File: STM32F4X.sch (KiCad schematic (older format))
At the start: 19 parts

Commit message: Added USB
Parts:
- added D?: LED, symbol Device:LED
- added J?: SWD_Conn, symbol Connector_Generic:Conn_02x05_Odd_Even
- added J?: USB_B_Micro, symbol Connector:USB_B_Micro
- added R?: 2K2, symbol Device:R_Small
- added U?: USBLC6-2SC6, Package_TO_SOT_SMD:SOT-23-6, symbol Power_Protection:USBLC6-2SC6
- R?: value 1K -> 2K2
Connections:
- net labels added: +5V, BOOT1, USB_CONN_DM, USB_CONN_DP
- wire segments 77 -> 94
- no-connect marks 0 -> 4
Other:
- note added: "SWD"
- note added: "USB Connection"
- moved on the sheet: C?, D?, R?, SW?, U?

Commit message: Initial board layout
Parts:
- removed C?: 2.2uF, symbol Device:C_Small
- removed D?: RED, symbol Device:LED_Small
- removed R?: 2K2, symbol Device:R_Small
- added C1, C10, C17: 100nF, Capacitor_SMD:C_0805_2012Metric_Pad1.18x1.45mm_HandSolder, symbol Device:C_Small
- added C2: 4.7uF, Capacitor_SMD:C_0805_2012Metric_Pad1.18x1.45mm_HandSolder, symbol Device:C_Small
- added C3: 10uF, Capacitor_SMD:C_0805_2012Metric_Pad1.18x1.45mm_HandSolder, symbol Device:C_Small
- added C4: 2.2uF, Capacitor_SMD:C_0805_2012Metric_Pad1.18x1.45mm_HandSolder, symbol Device:C_Small
- added D1, D3: B260A-13-F, Diode_SMD:D_0805_2012Metric_Pad1.15x1.40mm_HandSolder, symbol Device:D_Schottky
- added D2: LED_Small, LED_SMD:LED_0805_2012Metric_Pad1.15x1.40mm_HandSolder, symbol Device:LED_Small
- added F1, F2, F3: 500mA, Fuse:Fuse_1206_3216Metric_Pad1.42x1.75mm_HandSolder, symbol Device:Polyfuse_Small
- added J1: POW_IN, TerminalBlock:TerminalBlock_Wuerth_691311400102_P7.62mm, symbol Connector:Screw_Terminal_01x02
- added J4: Micro_SD_Card, Connector_Card:microSD_HC_Molex_104031-0811, symbol Connector:Micro_SD_Card
- added L1: 22uH, Inductor_SMD:L_1206_3216Metric_Pad1.42x1.75mm_HandSolder, symbol Device:L_Small
- added R1: 49.9K, Resistor_SMD:R_0805_2012Metric_Pad1.20x1.40mm_HandSolder, symbol Device:R_Small
- added R2: 15.8K, Resistor_SMD:R_0805_2012Metric_Pad1.20x1.40mm_HandSolder, symbol Device:R_Small
- added R3: 68K, Resistor_SMD:R_0805_2012Metric_Pad1.20x1.40mm_HandSolder, symbol Device:R_Small
- added R4: 2K2, Resistor_SMD:R_0805_2012Metric_Pad1.20x1.40mm_HandSolder, symbol Device:R_Small
- added U1: AOZ1282CI, Package_TO_SOT_SMD:SOT-23-6, symbol Regulator_Switching:AOZ1282CI
- C11, C12, C13, C14, C15, C16, C5, C6, C7, C8, C9: renamed from C?; footprint (none) -> Capacitor_SMD:C_0805_2012Metric_Pad1.18x1.45mm_HandSolder
- D4: renamed from D?; footprint (none) -> LED_SMD:LED_0805_2012Metric_Pad1.15x1.40mm_HandSolder
- FB1: renamed from FB?; footprint (none) -> Inductor_SMD:L_0805_2012Metric_Pad1.15x1.40mm_HandSolder
- J2: renamed from J?; footprint (none) -> Connector_USB:USB_Micro-B_Molex-105017-0001; symbol Connector:USB_B_Micro -> STM32F4X-rescue:USB_B_Micro-Connector
- J3: renamed from J?; footprint (none) -> Connector_PinHeader_2.54mm:PinHeader_2x05_P2.54mm_Vertical
- R5, R6: renamed from R?; footprint (none) -> Resistor_SMD:R_0805_2012Metric_Pad1.20x1.40mm_HandSolder
- SW1: renamed from SW?; footprint (none) -> digikey-footprints:Switch_Slide_11.6x4mm_EG1218
- U3: renamed from U?; symbol Power_Protection:USBLC6-2SC6 -> STM32F4X-rescue:USBLC6-2SC6-Power_Protection
- Y1: renamed from Y?; footprint (none) -> Oscillator:Oscillator_SMD_EuroQuartz_XO32-4Pin_3.2x2.5mm_HandSoldering
- gave numbers to parts that had none: 1
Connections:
- net labels added: BST, BUCK_OUT, FB, SDIO_CK, SDIO_CMD, SDIO_D0, SDIO_D1, SDIO_D2, SDIO_D3, SPI_CS, SPI_MISO, SPI_MOSI, SPI_SCLK, VBUS, VCC
- net labels removed: BOOT1, I2C2_SCL, I2C2_SDA, UART5_RX, UART5_TX
- wire segments 94 -> 134
- no-connect marks 4 -> 9
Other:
- note added: "Power Supply"
- note added: "SD_Card"
- note added: "The output voltage of the buck converter is set by:\n V_out = 0.8*(1+R1/R2)"
- moved on the sheet: C11, C12, C13, C14, C15, C16, C5, C6, C7, C8, C9, D4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

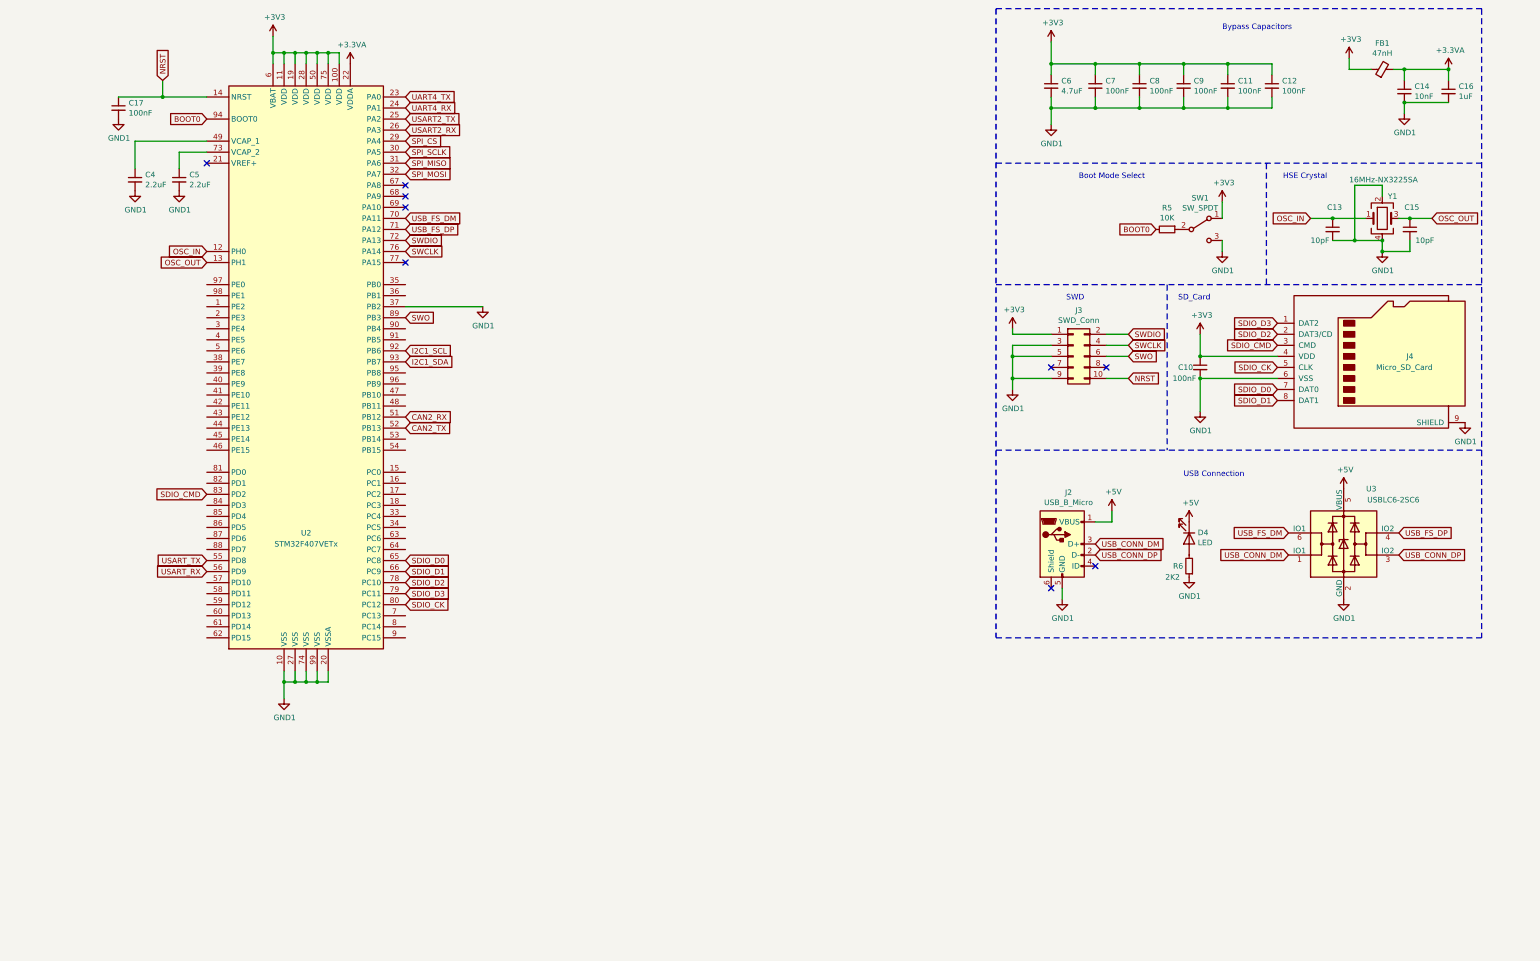
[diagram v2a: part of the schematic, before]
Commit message: Removed pcb layout. Adding more functionality
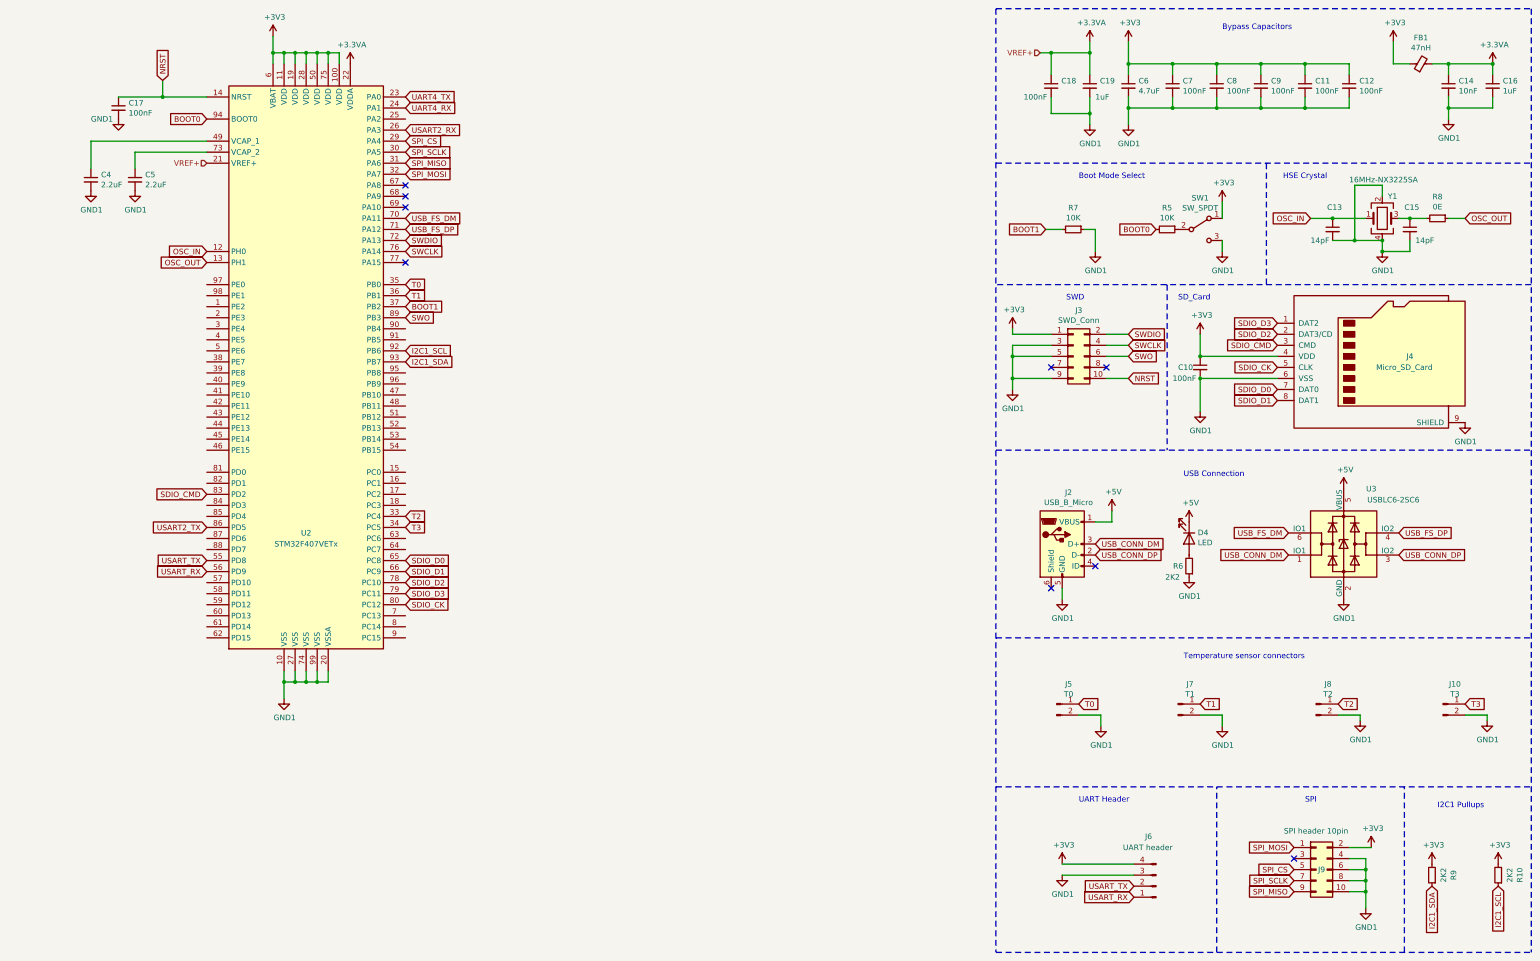
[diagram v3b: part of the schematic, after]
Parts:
- added C18: 100nF, Capacitor_SMD:C_0805_2012Metric_Pad1.18x1.45mm_HandSolder, symbol Device:C_Small
- added C19: 1uF, Capacitor_SMD:C_0805_2012Metric_Pad1.18x1.45mm_HandSolder, symbol Device:C_Small
- added J10: T3, symbol Connector:Conn_01x02_Male
- added J5: T0, symbol Connector:Conn_01x02_Male
- added J6: UART header, symbol Connector:Conn_01x04_Male
- added J7: T1, symbol Connector:Conn_01x02_Male
- added J8: T2, symbol Connector:Conn_01x02_Male
- added J9: SPI header 10pin, symbol Connector_Generic:Conn_02x05_Odd_Even
- added R10, R9: 2K2, Resistor_SMD:R_0805_2012Metric_Pad1.20x1.40mm_HandSolder, symbol Device:R_Small
- added R7: 10K, Resistor_SMD:R_0805_2012Metric_Pad1.20x1.40mm_HandSolder, symbol Device:R_Small
- added R8: 0E, Resistor_SMD:R_0805_2012Metric_Pad1.20x1.40mm_HandSolder, symbol Device:R_Small
- C13, C15: value 10pF -> 14pF
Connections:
- net +3.3VA: now also U2.21 (VREF+), C18.1, C19.1
- net +3V3: now also J6.4 (Pin_4), J9.2 (Pin_2), R10.2, R9.2
- net GND1: now also C18.2, C19.2, J10.2 (Pin_2), J5.2 (Pin_2), J6.3 (Pin_3), J7.2 (Pin_2), J8.2 (Pin_2), J9.10 (Pin_10), J9.4 (Pin_4), J9.6 (Pin_6), J9.8 (Pin_8), R7.1; no longer U2.37 (PB2)
- net I2C1_SCL: now also R10.1
- net I2C1_SDA: now also R9.1
- net OSC_OUT: now also R8.1; no longer C15.1, Y1.3
- net SPI_CS: now also J9.5 (Pin_5)
- net SPI_MISO: now also J9.9 (Pin_9)
- net SPI_MOSI: now also J9.1 (Pin_1)
- net SPI_SCLK: now also J9.7 (Pin_7)
- net USART2_TX: now also U2.86 (PD5); no longer U2.25 (PA2)
- net USART_RX: now also J6.1 (Pin_1)
- net USART_TX: now also J6.2 (Pin_2)
- net T2: now reaches U2.33 (PC4)
- net T2: now also J8.1 (Pin_1)
- net T3: now reaches U2.34 (PC5)
- net T3: now also J10.1 (Pin_1)
- net T0: now reaches U2.35 (PB0)
- net T0: now also J5.1 (Pin_1)
- net T1: now reaches U2.36 (PB1)
- net T1: now also J7.1 (Pin_1)
- net CAN2_RX: no longer names the net of U2.51 (PB12)
- net CAN2_TX: no longer names the net of U2.52 (PB13)
- new net: C15.1, R8.2, Y1.3
- new net BOOT1: R7.2, U2.37 (PB2)
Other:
- note added: "I2C1 Pullups\n"
- note added: "SPI\n"
- note added: "Temperature sensor connectors"
- note added: "UART Header\n"
- moved on the sheet: C11, C12, C14, C16, C4, C5, C6, C7, C8, C9, FB1

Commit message: Added, a proper 3v3 LDO from buck converter output. Started allocation for SPI and UART pins for motor drivers.
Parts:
- added A?: DRV8825_X, Module:Pololu_Breakout-16_15.2x20.3mm, symbol Driver_Motor:Pololu_Breakout_DRV8825
- added A?: A4988_Y, Module:Pololu_Breakout-16_15.2x20.3mm, symbol Driver_Motor:Pololu_Breakout_A4988
- added A?: Pololu_Breakout_TMC2209, Module:Pololu_Breakout-16_15.2x20.3mm, symbol Trinamic_breakout:Pololu_Breakout_TMC2209
- added A?: Pololu_Breakout_TMC2130, Module:Pololu_Breakout-16_15.2x20.3mm, symbol Trinamic_breakout:Pololu_Breakout_TMC2130
- added C20, C21, C22, C23, C24, C25: 10uF, Capacitor_SMD:C_0805_2012Metric_Pad1.18x1.45mm_HandSolder, symbol Device:C_Small
- added C? (x3): 100uF, 65V, symbol Device:CP_Small
- added C? (x2): 1uF, Capacitor_SMD:C_0805_2012Metric_Pad1.18x1.45mm_HandSolder, symbol Device:C_Small
- added J11: TC, symbol Connector:Conn_01x02_Male
- added J12: T3, symbol Connector:Conn_01x02_Male
- added J? (x3): Motor, symbol Connector:Conn_01x04_Female
- added R11, R12, R13, R14, R15, R16, R17, R? (x3): 10K, Resistor_SMD:R_0805_2012Metric_Pad1.20x1.40mm_HandSolder, symbol Device:R_Small
- added R18: 1M, Resistor_SMD:R_0805_2012Metric_Pad1.20x1.40mm_HandSolder, symbol Device:R_Small
- added R19, R20, R21, R22, R23, R24: 4K7, Resistor_SMD:R_0805_2012Metric_Pad1.20x1.40mm_HandSolder, symbol Device:R_Small
- added SW2: SW_RESET, symbol Switch:SW_DIP_x01
- added U?: TLV75533PDBV, Package_TO_SOT_SMD:SOT-23-5, symbol Regulator_Linear:TLV75533PDBV
- J10: value T3 -> T2
- J7: value T1 -> TB
- J8: value T2 -> T1
- R1: value 49.9K -> 47K
- R2: value 15.8K -> 10K
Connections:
- net +3V3: now also A?.2 (VDD), A?.2 (VIO), A?.2 (~FLT), R11.2, R12.2, R13.2, R14.2, R15.2, R16.2, R17.2, R19.1, R20.1, R21.1, R22.1, R23.1, R24.1, R?.2, R?.2, R?.2
- net GND1: now also A?.1 (GND), A?.1 (GND), A?.1 (GND), A?.7 (GND), A?.7 (GND), A?.7 (GND), C20.2, C21.2, C22.2, C23.2, C24.2, C25.2, C?.2, C?.2, C?.2, C?.2, C?.2, J11.2 (Pin_2), J12.2 (Pin_2), SW2.1, U?.2 (GND)
- net NRST: now also R11.1, SW2.2
- net OSC_IN: now also R18.2
- net OSC_OUT: now also R18.1
- net SDIO_CK: now also R15.1
- net SDIO_CMD: now also R14.1
- net SDIO_D0: now also R16.1
- net SDIO_D1: now also R17.1
- net SDIO_D2: now also J4.1 (DAT2), R12.1; no longer J4.2 (DAT3/CD)
- net SDIO_D3: now also J4.2 (DAT3/CD), R13.1; no longer J4.1 (DAT2)
- net T0: now also C20.1, R19.2
- net T1: now also J8.1 (Pin_1), C22.1, R21.2; no longer J7.1 (Pin_1)
- net T2: now also J10.1 (Pin_1), C23.1, R22.2; no longer J8.1 (Pin_1)
- net T3: now also C25.1, J12.1 (Pin_1), R24.2; no longer J10.1 (Pin_1)
- net VCC: now also A?.8 (VMOT), A?.8 (VMOT), A?.8 (VMOT), C?.1, C?.1, C?.1
- net SPI2_MISO: now reaches U2.17 (PC2)
- net T_CHAMBER: now reaches U2.18 (PC3)
- net T_CHAMBER: now also C24.1, J11.1 (Pin_1), R23.2
- net TB: now reaches U2.25 (PA2)
- net TB: now also J7.1 (Pin_1), C21.1, R20.2
- net SPI2_SCK: now reaches U2.52 (PB13)
- net SPI2_CS: now reaches U2.53 (PB14)
- net SPI2_MOSI: now reaches U2.54 (PB15)
- net at C3.1, L1.2, R1.2: now also C?.1, U?.1 (IN), U?.3 (EN); no longer F2.2
- new net: A?.13 (~RST), A?.14 (~SLP)
- new net: A?.3 (A2), J?.2 (Pin_2)
- new net: A?.4 (A1), J?.1 (Pin_1)
- new net: A?.5 (B1), J?.3 (Pin_3)
- new net: A?.6 (B2), J?.4 (Pin_4)
- new net: A?.9 (~EN), R?.1 (x2)
- new net: A?.13 (~RESET), A?.14 (~SLEEP)
- new net: A?.3 (1B), J?.1 (Pin_1)
- new net: A?.4 (1A), J?.2 (Pin_2)
- new net: A?.5 (2A), J?.3 (Pin_3)
- new net: A?.6 (2B), J?.4 (Pin_4)
- new net: A?.9 (~ENABLE), R?.1
- new net: C?.1, F2.2, U?.5 (OUT)
- new net: A?.3 (B2), J?.2 (Pin_2)
- new net: A?.4 (B1), J?.1 (Pin_1)
- new net: A?.5 (A1), J?.3 (Pin_3)
- new net: A?.6 (A2), J?.4 (Pin_4)
- new net CS: A?.12 (CFG3/CS)
- new net DIR: A?.16 (DIR)
- new net MS0_X: A?.10 (M0)
- new net MS0_Y: A?.10 (MS1)
- new net MS1_X: A?.11 (M1)
- new net MS1_Y: A?.11 (MS2)
- new net MS2_X: A?.12 (M2)
- new net MS2_Y: A?.12 (MS3)
- new net STEP: A?.15 (STEP)
- new net mMISO: A?.13 (CFG0/SDO)
- new net mMOSI: A?.10 (CFG1/SDI)
- new net mSCK: A?.11 (CFG2/SCK)
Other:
- note added: "Heatbed And Chamber thermistors"
- note added: "Power Supply (microcontroller)"
- note added: "TLV75533PDBV requires atleast 0.47uF output capacitor"
- note added: "Toolhead thermistor connectors"
- note removed: "Power Supply"
- note removed: "Temperature sensor connectors"
- moved on the sheet: C10, C13, C15, C17, C4, C5, D2, D4, F2, J2, J3, J4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
